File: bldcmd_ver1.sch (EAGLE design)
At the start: 83 parts, among them IC1 STSPIN32F0, IC2 AS5047P-ATSM, IC3 ADM4852ACPZ-REEL7, J1 DF65-3P-1.7V(21), Q1 PSMN2R4-30MLD, Q2 PSMN2R4-30MLD, Q3 PSMN2R4-30MLD, Q4 PSMN2R4-30MLD, Q5 PSMN2R4-30MLD, Q6 PSMN2R4-30MLD

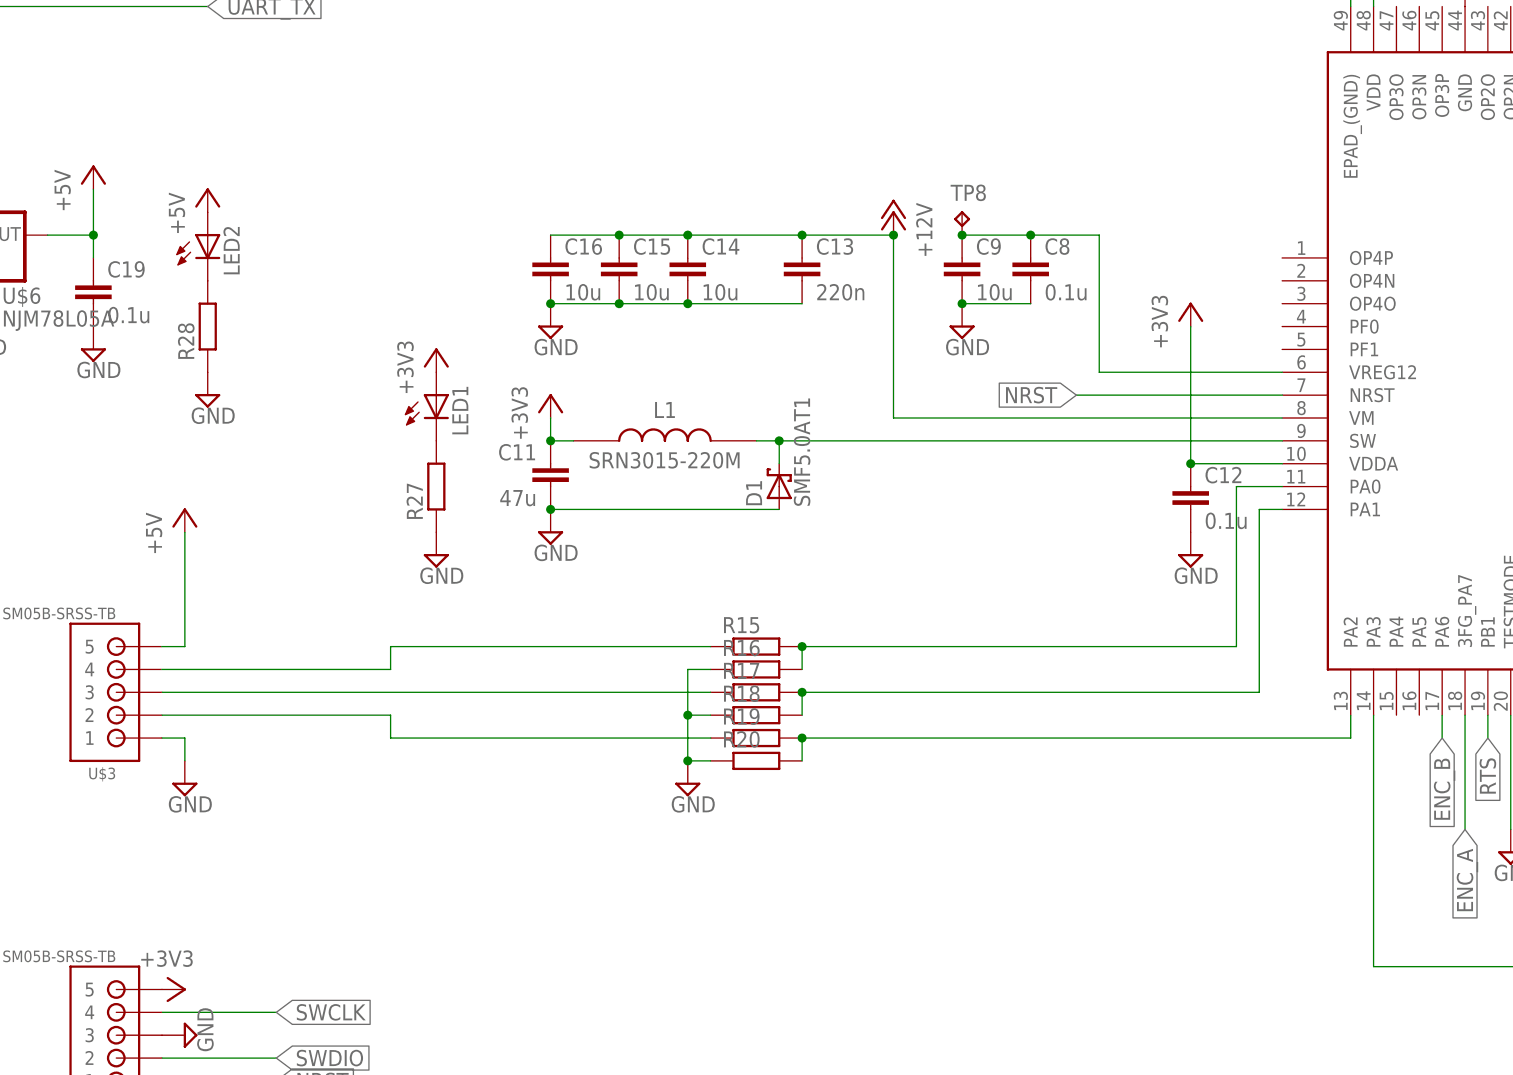
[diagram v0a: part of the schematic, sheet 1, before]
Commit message: コンデンサ増やした
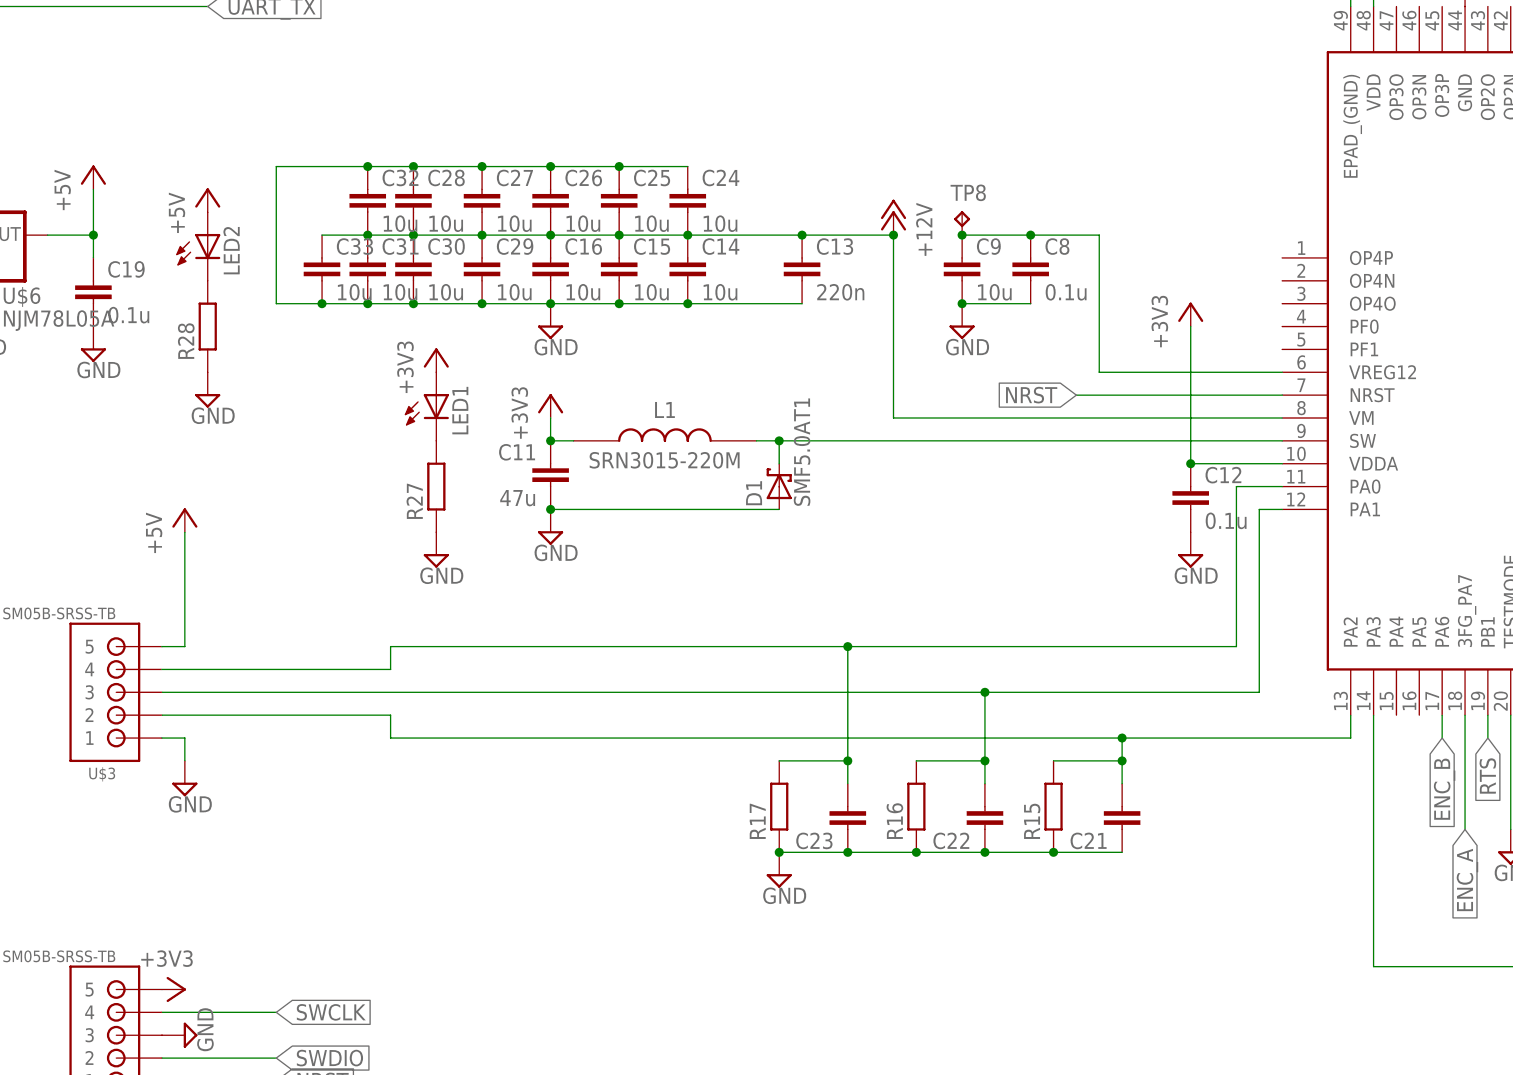
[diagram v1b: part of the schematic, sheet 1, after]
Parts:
- removed R18, R19, R20: (no value), rcl:R-EU_R0402
- added C21, C22, C23: (no value), rcl:C-EUC0402
- added C24, C25, C26, C27, C28, C29, C30, C31, C32, C33: 10u, rcl:C-EUC3216
- C14, C15, C16: device rcl:C-EUC3225 -> rcl:C-EUC3216
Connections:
- removed net N$20: IC1.PA0, R15.2, R16.2
- removed net N$21: IC1.PA1, R17.2, R18.2
- removed net N$22: IC1.PA2, R19.2, R20.2
- net +12V: now also C24.2, C25.2, C26.2, C27.2, C28.2, C29.1, C30.1, C31.1, C32.2, C33.1
- net GND: now also C21.1, C22.1, C23.1, C24.1, C25.1, C26.1, C27.1, C28.1, C29.2, C30.2, C31.2, C32.1, C33.2, R15.1, R17.1; no longer R18.1, R20.1
- net N$23: now also C21.2, IC1.PA2, R15.2; no longer R19.1
- net N$24: now also C22.2, IC1.PA1, R16.2; no longer R17.1
- net N$25: now also C23.2, IC1.PA0, R17.2; no longer R15.1
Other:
- moved on the sheet: R15, R16, R17

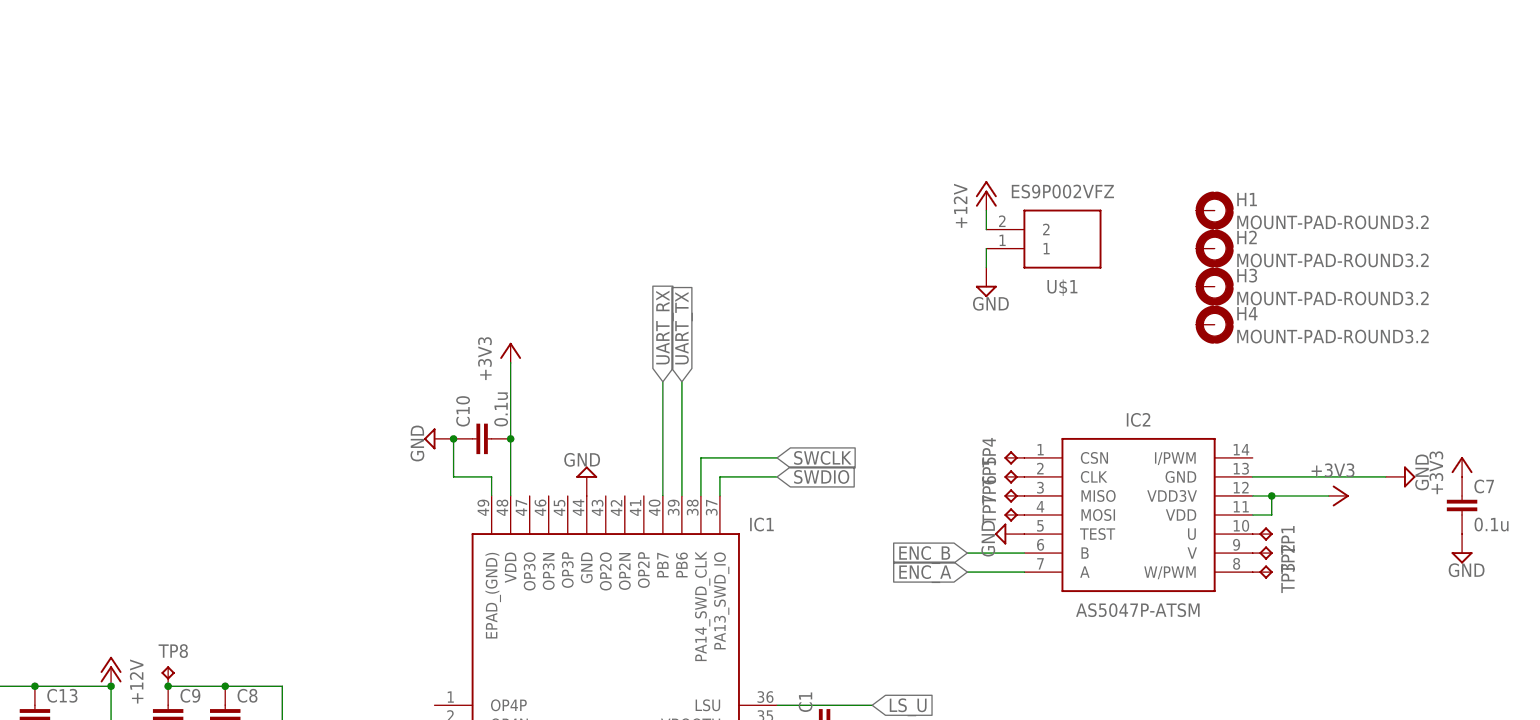
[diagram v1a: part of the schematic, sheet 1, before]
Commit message: シルクの位置調整
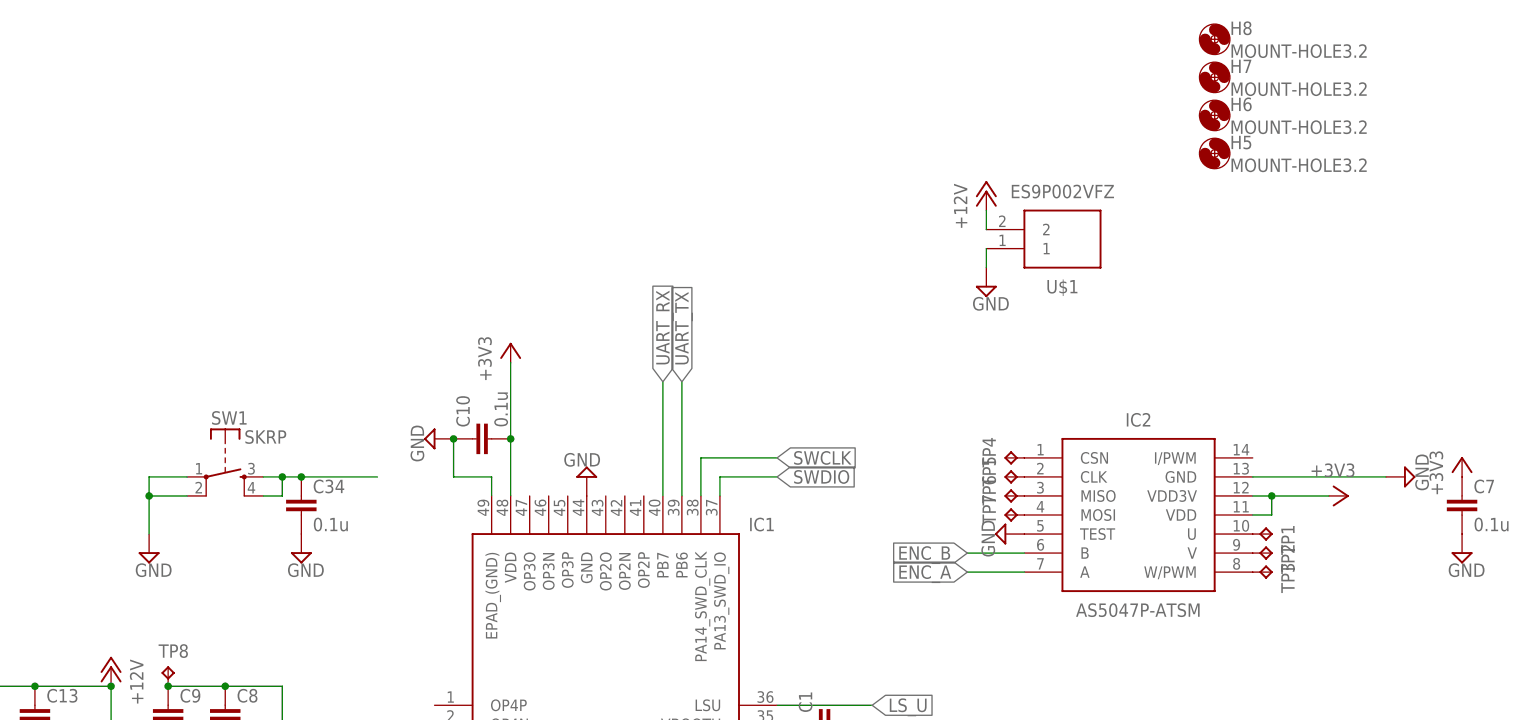
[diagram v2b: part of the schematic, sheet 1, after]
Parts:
- removed H1, H2, H3, H4: MOUNT-PAD-ROUND3.2, holes:MOUNT-PAD-ROUND3.2
- added C34: 0.1u, rcl:C-EUC0603K
- added H5, H6, H7, H8: MOUNT-HOLE3.2, holes:MOUNT-HOLE3.2
- added SW1: SKRP, 0_Yuki_Lib:SKRP
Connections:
- net GND: now also C34.2, SW1.1, SW1.2
- net NRST: now also C34.1, SW1.3, SW1.4
